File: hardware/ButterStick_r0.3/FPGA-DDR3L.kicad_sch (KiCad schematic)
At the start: 1 part, among them U2 ECP5UM5G_85_CABGA381

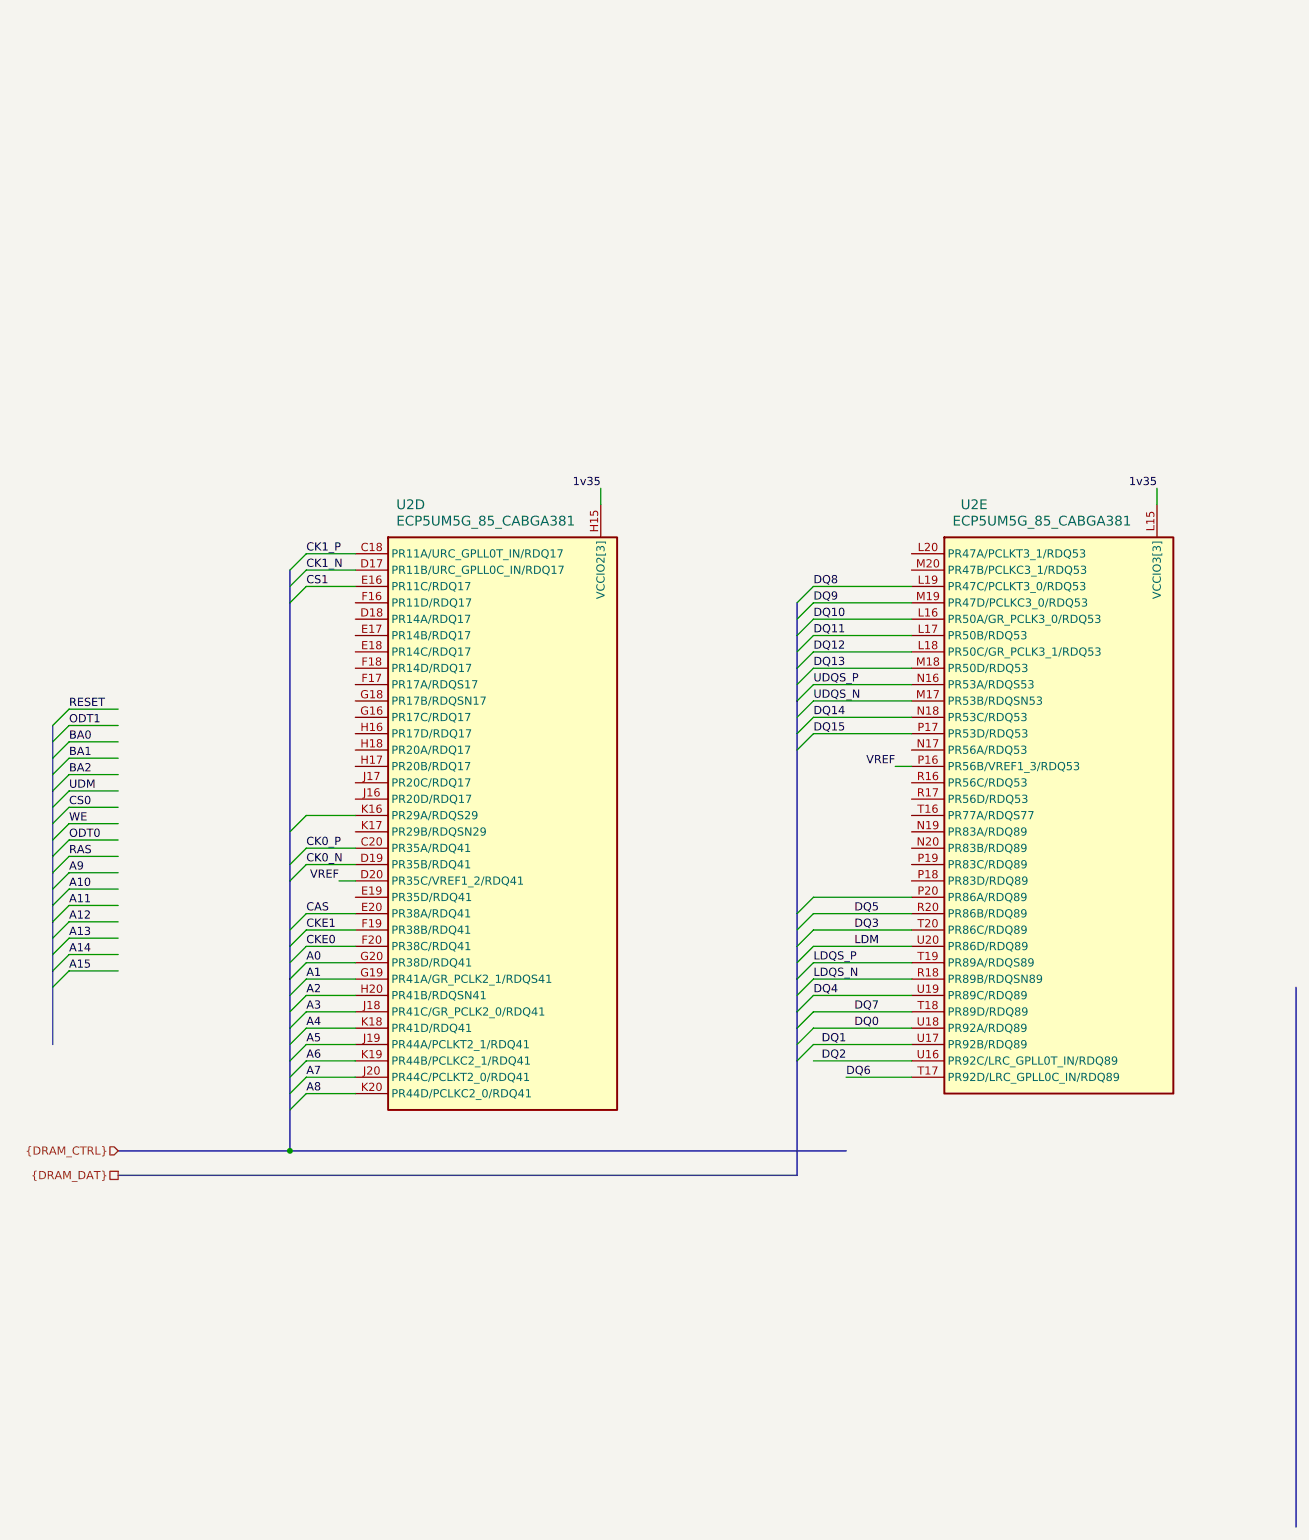
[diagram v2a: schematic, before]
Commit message: hw.r0_3: Inital routing of DDR3 done
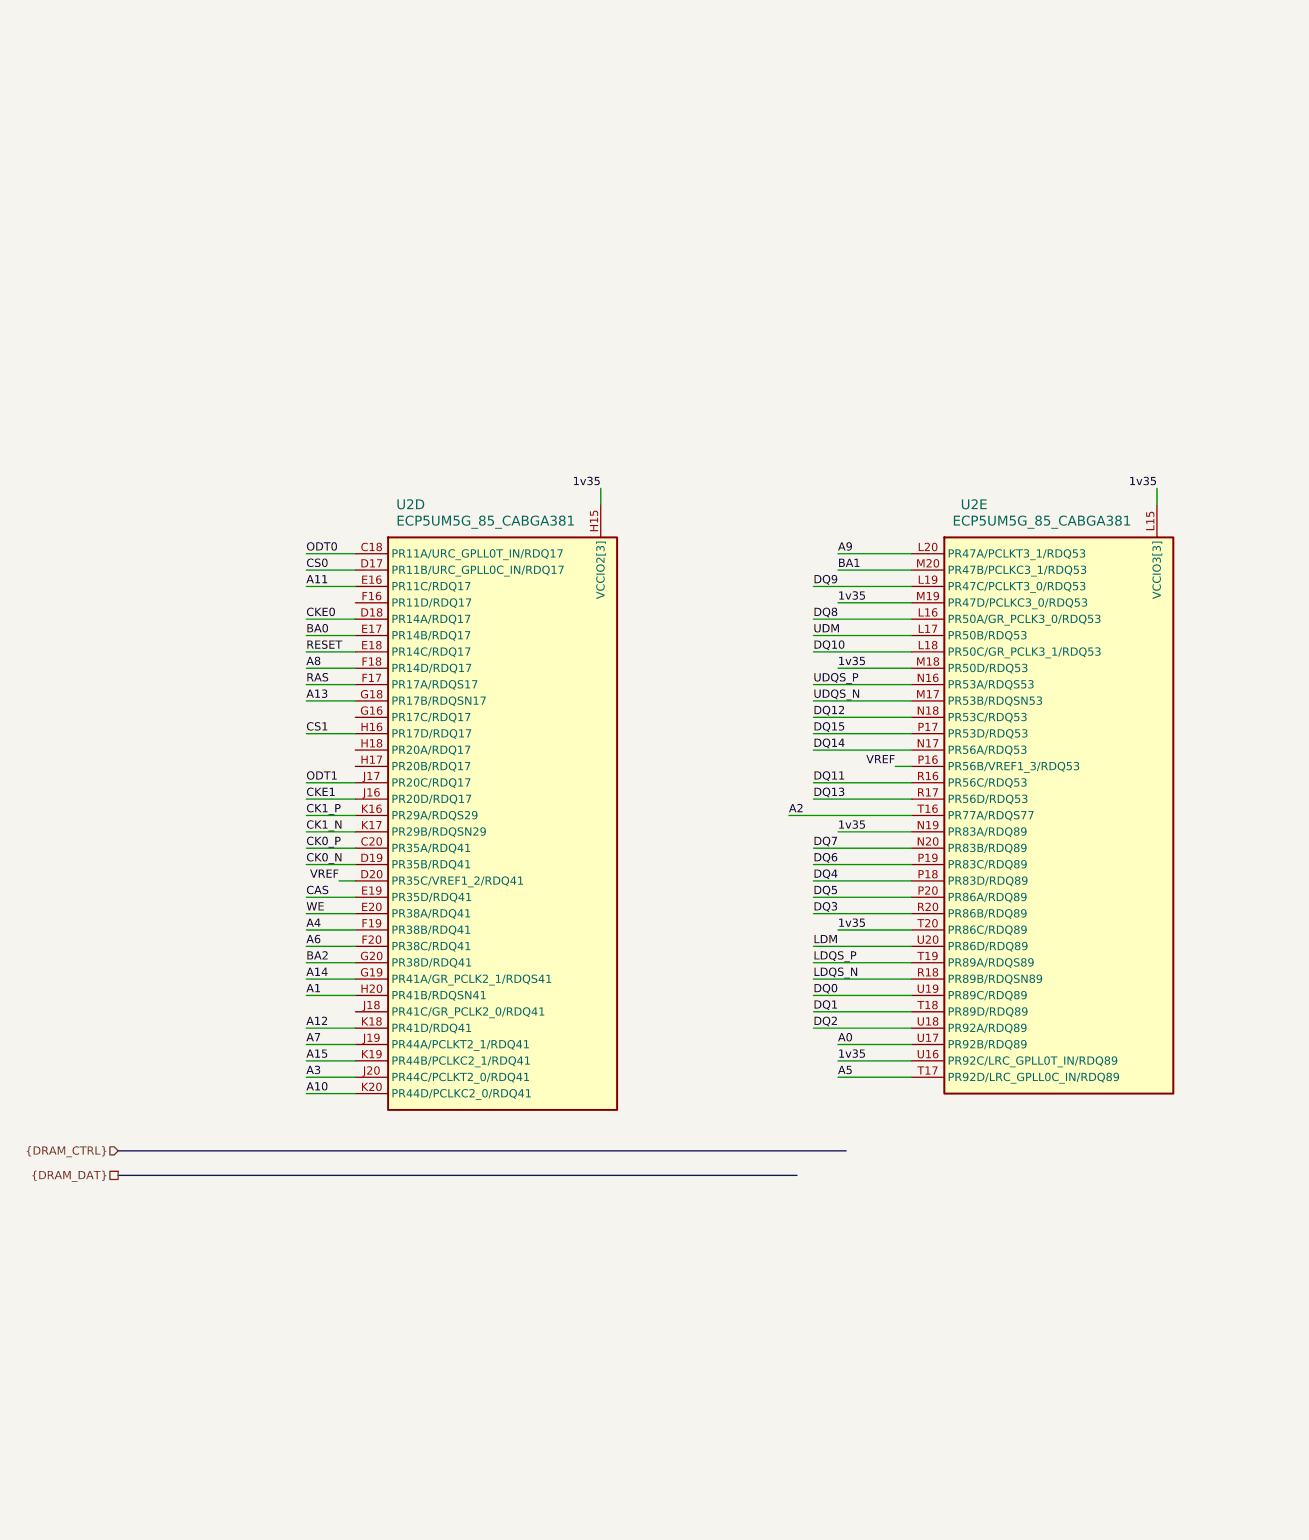
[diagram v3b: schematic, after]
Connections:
- net 1v35: now also U2.M18 (PR50D/RDQ53), U2.M19 (PR47D/PCLKC3_0/RDQ53), U2.N19 (PR83A/RDQ89), U2.T20 (PR86C/RDQ89), U2.U16 (PR92C/LRC_GPLL0T_IN/RDQ89)
- net A0: now also U2.U17 (PR92B/RDQ89); no longer U2.G20 (PR38D/RDQ41)
- net A1: now also U2.H20 (PR41B/RDQSN41); no longer U2.G19 (PR41A/GR_PCLK2_1/RDQS41)
- net A10: now also U2.K20 (PR44D/PCLKC2_0/RDQ41)
- net A11: now also U2.E16 (PR11C/RDQ17)
- net A12: now also U2.K18 (PR41D/RDQ41)
- net A13: now also U2.G18 (PR17B/RDQSN17)
- net A14: now also U2.G19 (PR41A/GR_PCLK2_1/RDQS41)
- net A15: now also U2.K19 (PR44B/PCLKC2_1/RDQ41)
- net A2: now also U2.T16 (PR77A/RDQS77); no longer U2.H20 (PR41B/RDQSN41)
- net A3: now also U2.J20 (PR44C/PCLKT2_0/RDQ41); no longer U2.J18 (PR41C/GR_PCLK2_0/RDQ41)
- net A4: now also U2.F19 (PR38B/RDQ41); no longer U2.K18 (PR41D/RDQ41)
- net A5: now also U2.T17 (PR92D/LRC_GPLL0C_IN/RDQ89); no longer U2.J19 (PR44A/PCLKT2_1/RDQ41)
- net A6: now also U2.F20 (PR38C/RDQ41); no longer U2.K19 (PR44B/PCLKC2_1/RDQ41)
- net A7: now also U2.J19 (PR44A/PCLKT2_1/RDQ41); no longer U2.J20 (PR44C/PCLKT2_0/RDQ41)
- net A8: now also U2.F18 (PR14D/RDQ17); no longer U2.K20 (PR44D/PCLKC2_0/RDQ41)
- net A9: now also U2.L20 (PR47A/PCLKT3_1/RDQ53)
- net BA0: now also U2.E17 (PR14B/RDQ17)
- net BA1: now also U2.M20 (PR47B/PCLKC3_1/RDQ53)
- net BA2: now also U2.G20 (PR38D/RDQ41)
- net CAS: now also U2.E19 (PR35D/RDQ41); no longer U2.E20 (PR38A/RDQ41)
- net CK1_N: now also U2.K17 (PR29B/RDQSN29); no longer U2.D17 (PR11B/URC_GPLL0C_IN/RDQ17)
- net CK1_P: now also U2.K16 (PR29A/RDQS29); no longer U2.C18 (PR11A/URC_GPLL0T_IN/RDQ17)
- net CKE0: now also U2.D18 (PR14A/RDQ17); no longer U2.F20 (PR38C/RDQ41)
- net CKE1: now also U2.J16 (PR20D/RDQ17); no longer U2.F19 (PR38B/RDQ41)
- net CS0: now also U2.D17 (PR11B/URC_GPLL0C_IN/RDQ17)
- net CS1: now also U2.H16 (PR17D/RDQ17); no longer U2.E16 (PR11C/RDQ17)
- net DQ0: now also U2.U19 (PR89C/RDQ89); no longer U2.U18 (PR92A/RDQ89)
- net DQ1: now also U2.T18 (PR89D/RDQ89); no longer U2.U17 (PR92B/RDQ89)
- net DQ10: now also U2.L18 (PR50C/GR_PCLK3_1/RDQ53); no longer U2.L16 (PR50A/GR_PCLK3_0/RDQ53)
- net DQ11: now also U2.R16 (PR56C/RDQ53); no longer U2.L17 (PR50B/RDQ53)
- net DQ12: now also U2.N18 (PR53C/RDQ53); no longer U2.L18 (PR50C/GR_PCLK3_1/RDQ53)
- net DQ13: now also U2.R17 (PR56D/RDQ53); no longer U2.M18 (PR50D/RDQ53)
- net DQ14: now also U2.N17 (PR56A/RDQ53); no longer U2.N18 (PR53C/RDQ53)
- net DQ2: now also U2.U18 (PR92A/RDQ89); no longer U2.U16 (PR92C/LRC_GPLL0T_IN/RDQ89)
- net DQ3: now also U2.R20 (PR86B/RDQ89); no longer U2.T20 (PR86C/RDQ89)
- net DQ4: now also U2.P18 (PR83D/RDQ89); no longer U2.U19 (PR89C/RDQ89)
- net DQ5: now also U2.P20 (PR86A/RDQ89); no longer U2.R20 (PR86B/RDQ89)
- net DQ6: now also U2.P19 (PR83C/RDQ89); no longer U2.T17 (PR92D/LRC_GPLL0C_IN/RDQ89)
- net DQ7: now also U2.N20 (PR83B/RDQ89); no longer U2.T18 (PR89D/RDQ89)
- net DQ8: now also U2.L16 (PR50A/GR_PCLK3_0/RDQ53); no longer U2.L19 (PR47C/PCLKT3_0/RDQ53)
- net DQ9: now also U2.L19 (PR47C/PCLKT3_0/RDQ53); no longer U2.M19 (PR47D/PCLKC3_0/RDQ53)
- net ODT0: now also U2.C18 (PR11A/URC_GPLL0T_IN/RDQ17)
- net ODT1: now also U2.J17 (PR20C/RDQ17)
- net RAS: now also U2.F17 (PR17A/RDQS17)
- net RESET: now also U2.E18 (PR14C/RDQ17)
- net UDM: now also U2.L17 (PR50B/RDQ53)
- net WE: now also U2.E20 (PR38A/RDQ41)

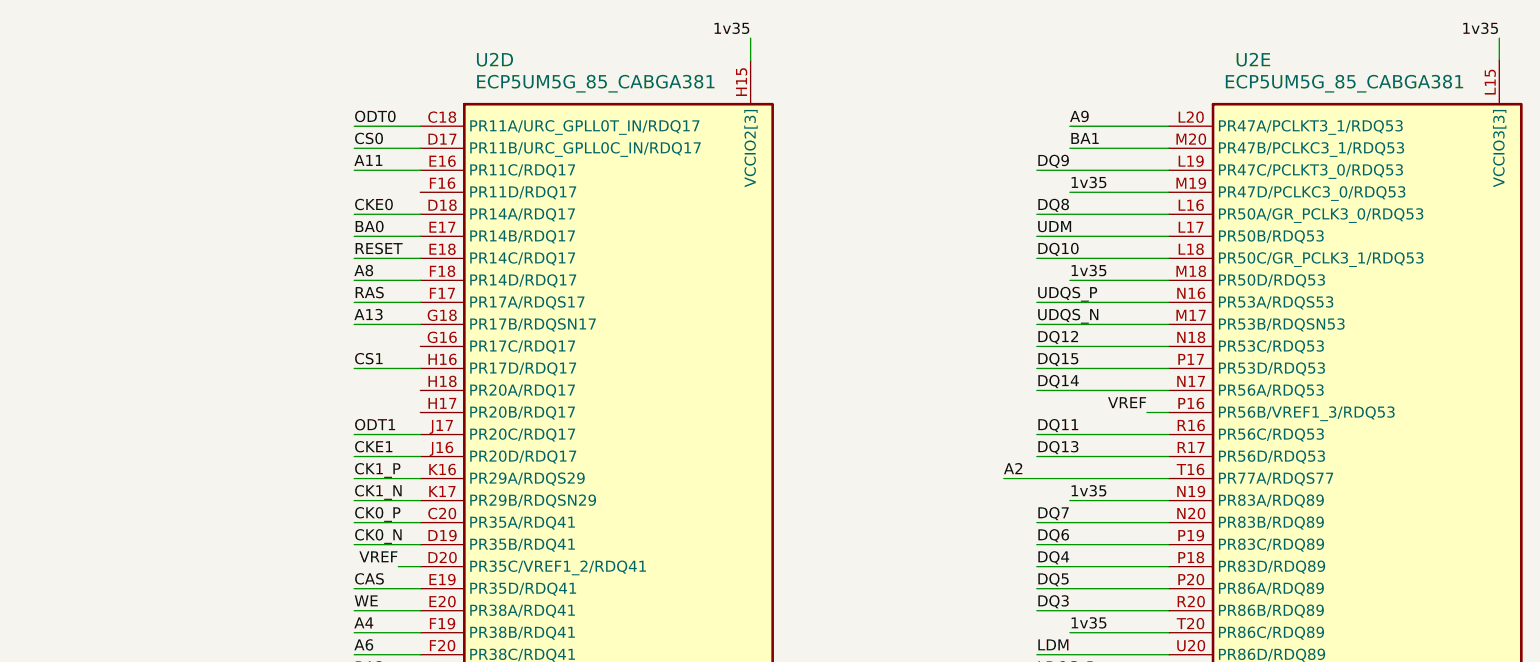
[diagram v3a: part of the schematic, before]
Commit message: hw.r0_3: routed SYZYGY, begin routing RGMII/ULPI
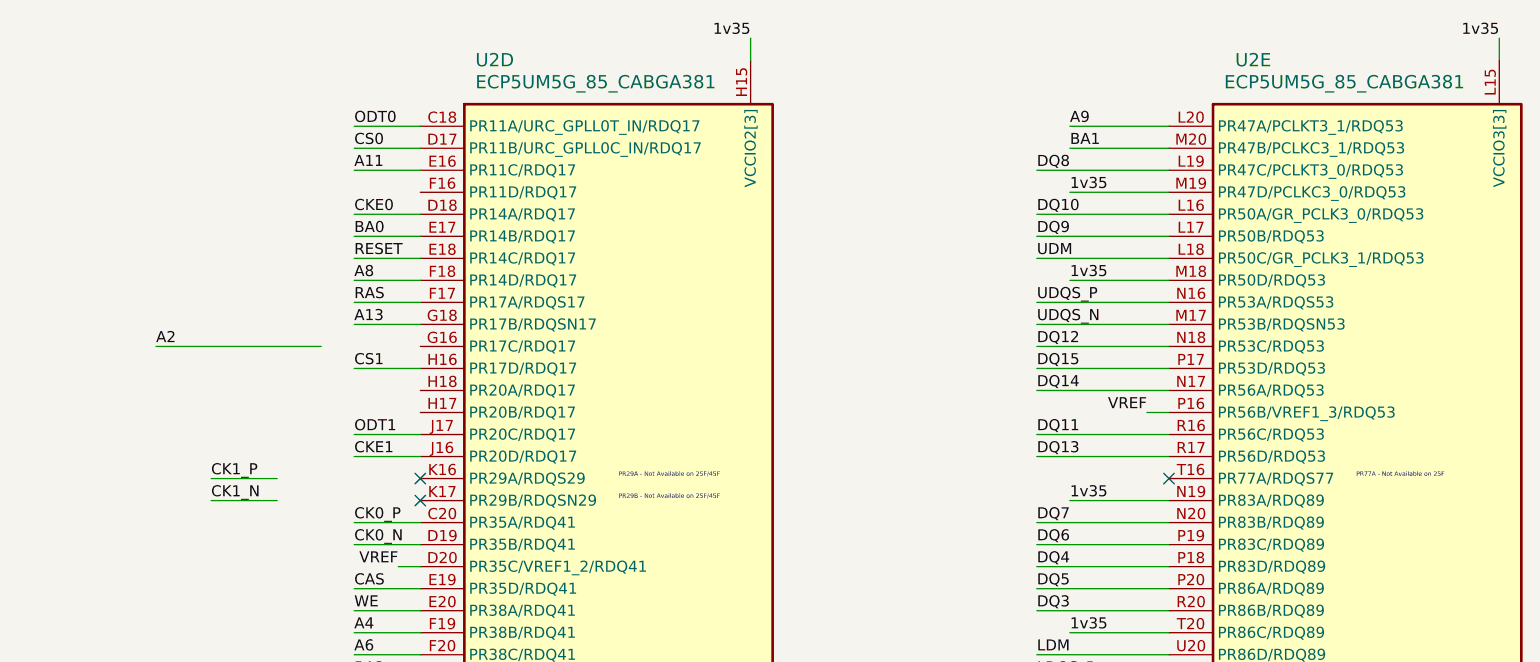
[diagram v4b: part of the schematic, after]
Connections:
- net A2: no longer U2.T16 (PR77A/RDQS77)
- net CK1_N: no longer U2.K17 (PR29B/RDQSN29)
- net CK1_P: no longer U2.K16 (PR29A/RDQS29)
- net DQ10: now also U2.L16 (PR50A/GR_PCLK3_0/RDQ53); no longer U2.L18 (PR50C/GR_PCLK3_1/RDQ53)
- net DQ8: now also U2.L19 (PR47C/PCLKT3_0/RDQ53); no longer U2.L16 (PR50A/GR_PCLK3_0/RDQ53)
- net DQ9: now also U2.L17 (PR50B/RDQ53); no longer U2.L19 (PR47C/PCLKT3_0/RDQ53)
- net UDM: now also U2.L18 (PR50C/GR_PCLK3_1/RDQ53); no longer U2.L17 (PR50B/RDQ53)
- no-connect marks 0 -> 3
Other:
- note added: "PR29A - Not Available on 25F/45F"
- note added: "PR29B - Not Available on 25F/45F"
- note added: "PR77A - Not Available on 25F"
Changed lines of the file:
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@@
 (kicad_sch (version 20200512) (host eeschema "5.99.0-unknown-711fc99~101~ubuntu18.04.1")
-  (page 9 20)
+  (page 8 19)
   (paper "A4")
+  (no_connect (at 90.17 97.79))
+  (no_connect (at 176.53 95.25))
+  (no_connect (at 90.17 95.25))
+  (wire (pts (xy 59.69 80.01) (xy 78.74 80.01)))
+  (wire (pts (xy 66.04 95.25) (xy 73.66 95.25)))
+  (wire (pts (xy 66.04 97.79) (xy 73.66 97.79)))
   (wire (pts (xy 82.55 54.61) (xy 90.17 54.61)))
   (wire (pts (xy 82.55 57.15) (xy 90.17 57.15)))
@@
   (wire (pts (xy 82.55 90.17) (xy 90.17 90.17)))
   (wire (pts (xy 82.55 92.71) (xy 90.17 92.71)))
-  (wire (pts (xy 82.55 95.25) (xy 90.17 95.25)))
-  (wire (pts (xy 82.55 97.79) (xy 90.17 97.79)))
   (wire (pts (xy 82.55 100.33) (xy 90.17 100.33)))
   (wire (pts (xy 82.55 102.87) (xy 90.17 102.87)))
@@
   (wire (pts (xy 87.63 105.41) (xy 90.17 105.41)))
   (wire (pts (xy 128.27 44.45) (xy 128.27 46.99)))
-  (wire (pts (xy 157.48 95.25) (xy 176.53 95.25)))
   (wire (pts (xy 161.29 59.69) (xy 176.53 59.69)))
   (wire (pts (xy 161.29 64.77) (xy 176.53 64.77)))
@@
   (bus (pts (xy 53.34 147.32) (xy 166.37 147.32)))
   (bus (pts (xy 53.34 151.13) (xy 158.75 151.13)))
+  (text "PR29A - Not Available on 25F/45F" (at 113.03 95.25 0)
+    (effects (font (size 0.508 0.508)) (justify left bottom))
+  )
+  (text "PR29B - Not Available on 25F/45F" (at 113.03 97.79 0)
+    (effects (font (size 0.508 0.508)) (justify left bottom))
+  )
+  (text "PR77A - Not Available on 25F" (at 198.12 95.25 0)
+    (effects (font (size 0.508 0.508)) (justify left bottom))
+  )
+  (label "A2" (at 59.69 80.01 0)
+    (effects (font (size 1.27 1.27)) (justify left bottom))
+  )
+  (label "CK1_P" (at 66.04 95.25 0)
+    (effects (font (size 1.27 1.27)) (justify left bottom))
+  )
+  (label "CK1_N" (at 66.04 97.79 0)
+    (effects (font (size 1.27 1.27)) (justify left bottom))
+  )
   (label "ODT0" (at 82.55 54.61 0)
     (effects (font (size 1.27 1.27)) (justify left bottom))
@@
   )
   (label "CKE1" (at 82.55 92.71 0)
-    (effects (font (size 1.27 1.27)) (justify left bottom))
-  )
-  (label "CK1_P" (at 82.55 95.25 0)
-    (effects (font (size 1.27 1.27)) (justify left bottom))
-  )
-  (label "CK1_N" (at 82.55 97.79 0)
     (effects (font (size 1.27 1.27)) (justify left bottom))
   )
@@
     (effects (font (size 1.27 1.27)) (justify right bottom))
   )
-  (label "A2" (at 157.48 95.25 0)
+  (label "DQ8" (at 161.29 59.69 0)
     (effects (font (size 1.27 1.27)) (justify left bottom))
   )
-  (label "DQ9" (at 161.29 59.69 0)
+  (label "DQ10" (at 161.29 64.77 0)
     (effects (font (size 1.27 1.27)) (justify left bottom))
   )
-  (label "DQ8" (at 161.29 64.77 0)
+  (label "DQ9" (at 161.29 67.31 0)
     (effects (font (size 1.27 1.27)) (justify left bottom))
   )
-  (label "UDM" (at 161.29 67.31 0)
+  (label "UDM" (at 161.29 69.85 0)
     (effects (font (size 1.27 1.27)) (justify left bottom))
   )
-  (label "DQ10" (at 161.29 69.85 0)
-    (effects (font (size 1.27 1.27)) (justify left bottom))
-  )
